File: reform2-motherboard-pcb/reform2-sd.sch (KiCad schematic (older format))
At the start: 13 parts, among them J3 SD_Card, U28 SN74AVC1T45, U8 TXS0108EPW

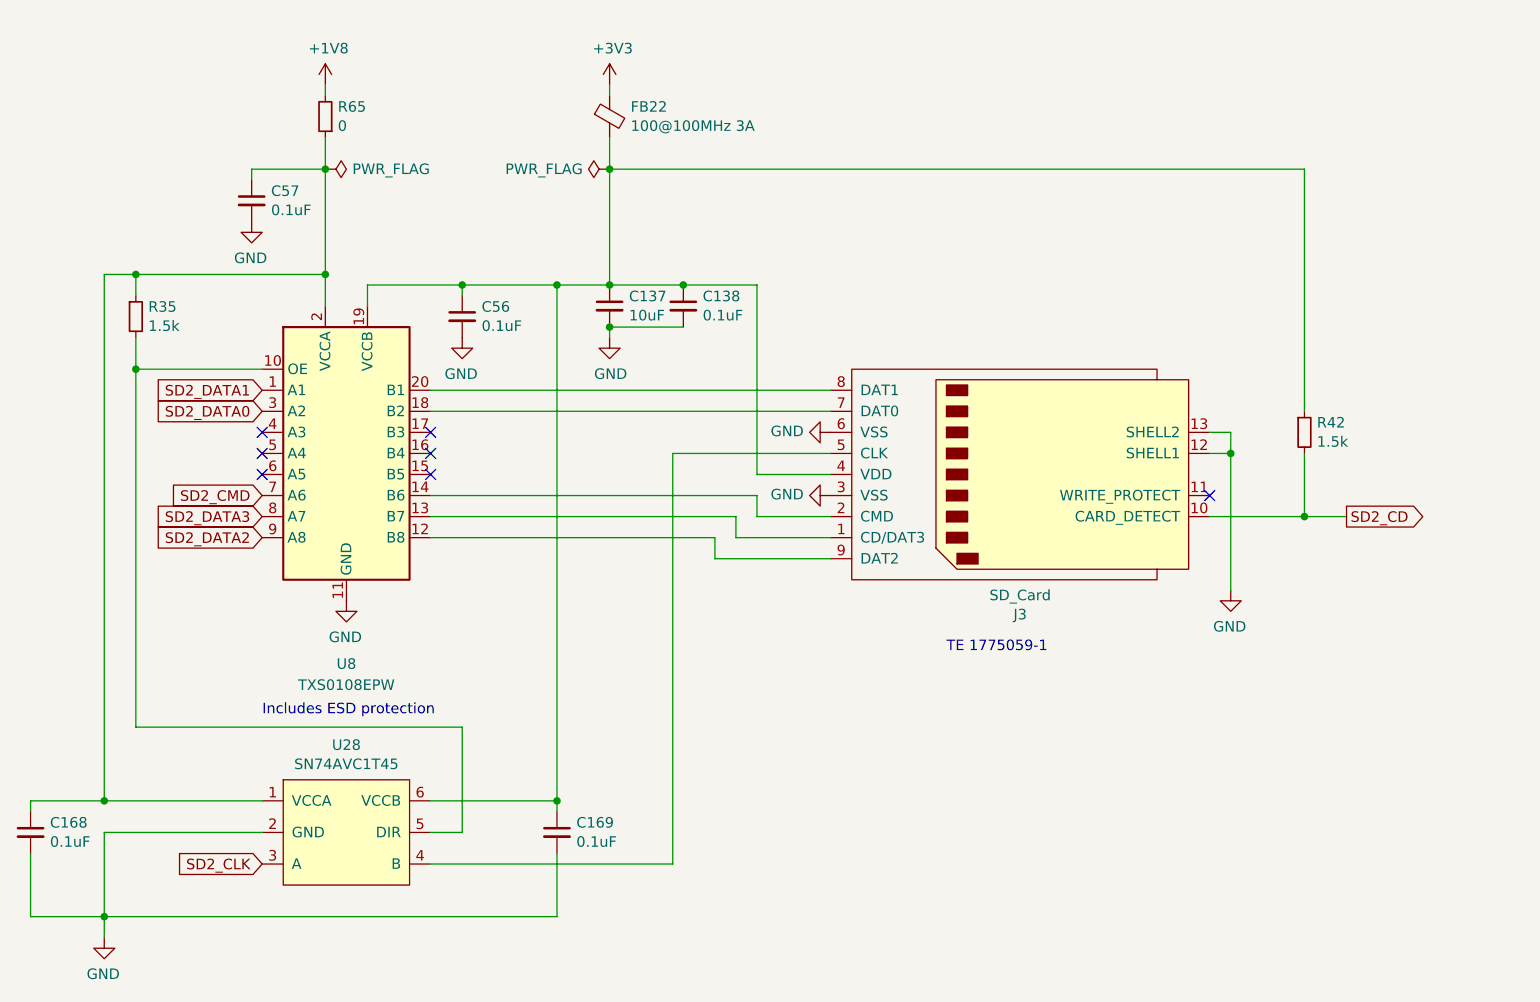
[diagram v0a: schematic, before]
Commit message: motherboard: add the split-up and cleaned up schematics that were made for the book
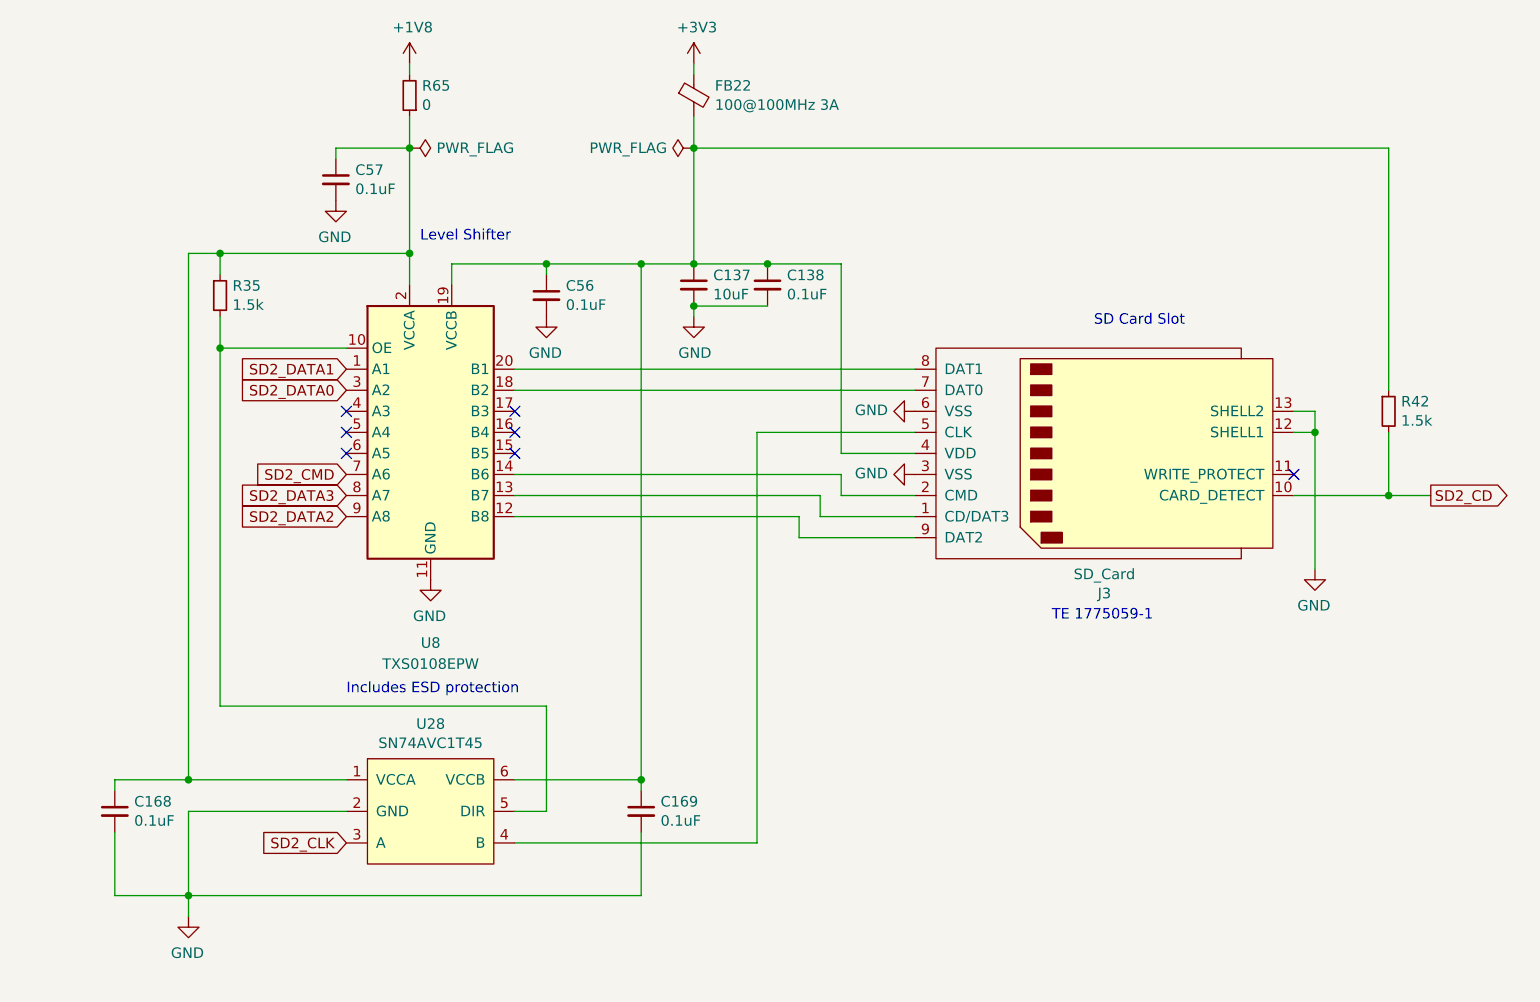
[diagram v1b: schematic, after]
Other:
- note added: "Level Shifter"
- note added: "SD Card Slot"
- moved on the sheet: C137, C138, C168, C169, C56, C57, FB22, J3, R35, R42, R65, U28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
